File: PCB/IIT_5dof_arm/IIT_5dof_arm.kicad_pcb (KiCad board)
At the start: 2 copper layers, 71.1 x 100 mm, 33 parts, among them J1 Screw_Terminal_01x02, J14 Conn_02x13_Top_Bottom, J8 Conn_01x04, SW1 SW_MAIN, SW15 SW_MOT, U5 XL8574T, U7 SN74LV1T34DBV, U8 SN74LV1T34DBV, U9 4504

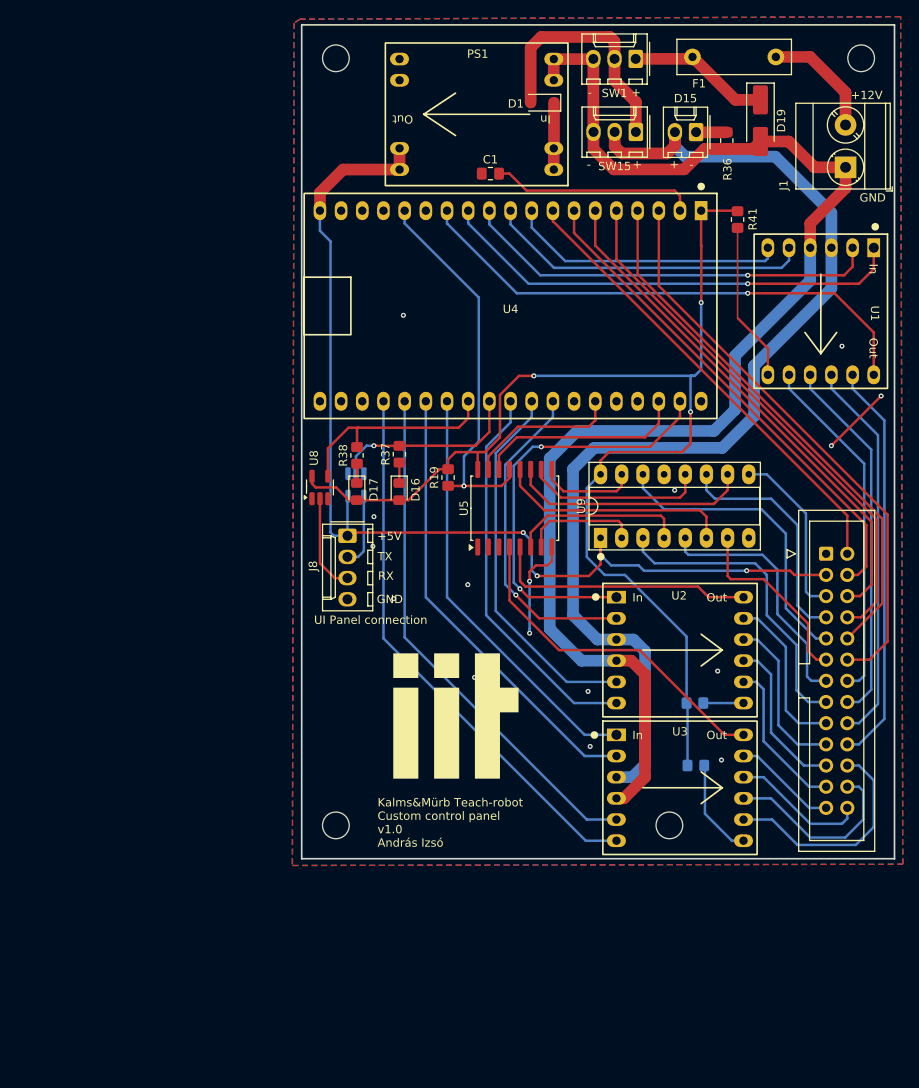
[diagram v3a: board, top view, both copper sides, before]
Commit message: implement RS232
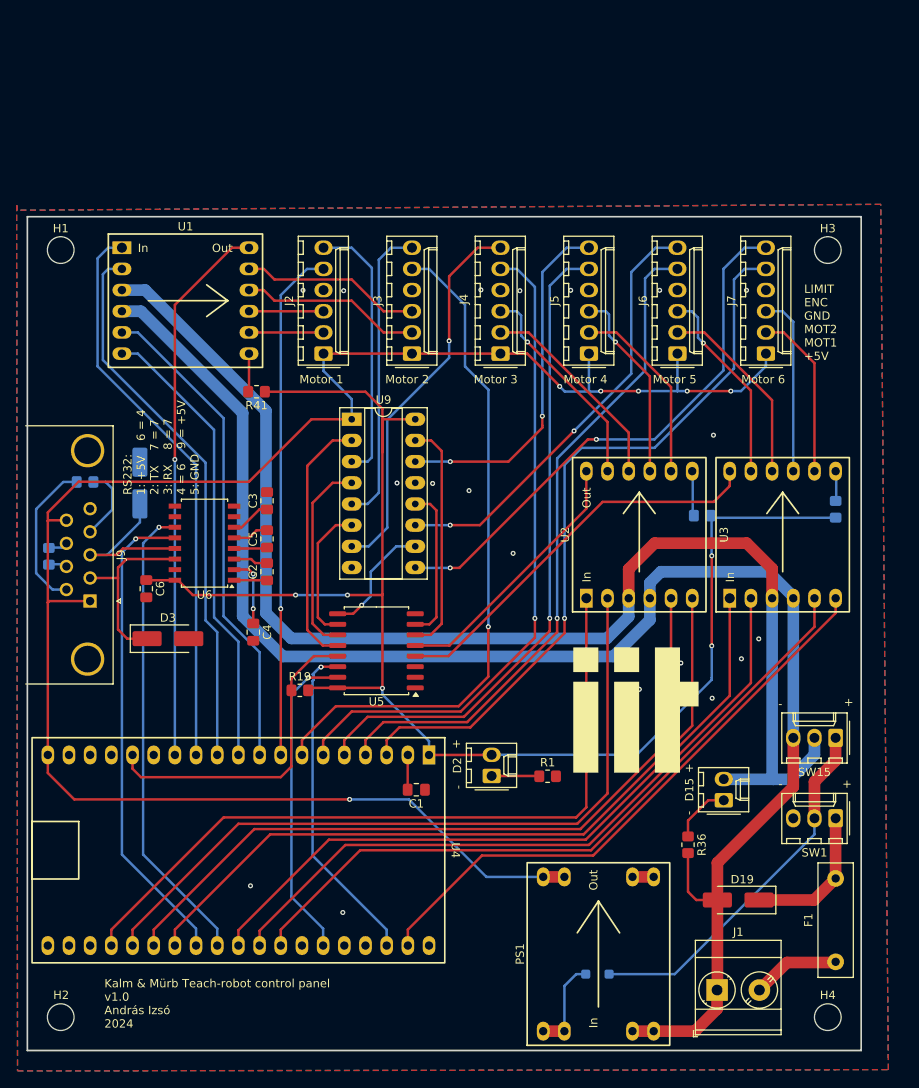
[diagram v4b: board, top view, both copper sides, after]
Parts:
- removed D16, D17: LED, LED_SMD:LED_0805_2012Metric_Pad1.15x1.40mm_HandSolder
- removed J14: Conn_02x13_Top_Bottom, Connector_IDC:IDC-Header_2x13_P2.54mm_Vertical
- removed J8: Conn_01x04, Connector_Molex:Molex_KK-254_AE-6410-04A_1x04_P2.54mm_Vertical
- removed R37, R38: 220, Resistor_SMD:R_0805_2012Metric_Pad1.20x1.40mm_HandSolder
- removed REF** (x4): MountingHole_3.2mm_M3, MountingHole:MountingHole_3.2mm_M3
- removed U7, U8: SN74LV1T34DBV, Package_TO_SOT_SMD:SOT-23-5_HandSoldering
- added C2: 0.1uF, Capacitor_SMD:C_0805_2012Metric_Pad1.18x1.45mm_HandSolder, F.Cu at (78.7, 92.6)
- added C3: 0.1uF, Capacitor_SMD:C_0805_2012Metric_Pad1.18x1.45mm_HandSolder, F.Cu at (78.7, 84.1)
- added C4: 0.1uF, Capacitor_SMD:C_0805_2012Metric_Pad1.18x1.45mm_HandSolder, F.Cu at (77.1, 99.8)
- added C5: 0.1uF, Capacitor_SMD:C_0805_2012Metric_Pad1.18x1.45mm_HandSolder, F.Cu at (78.7, 88.6)
- added C6: 0.1uF, Capacitor_SMD:C_0805_2012Metric_Pad1.18x1.45mm_HandSolder, F.Cu at (64.3, 94.6)
- added D2: LED, Connector_Molex:Molex_KK-254_AE-6410-02A_1x02_P2.54mm_Vertical, F.Cu at (105.7, 117.1)
- added D3: SMAJ12A, Diode_SMD:D_SMA_Handsoldering, F.Cu at (66.9, 100.6)
- added D4: SMAJ12A, Diode_SMD:D_SMA_Handsoldering, B.Cu at (63.5, 81.9)
- added H1: MountingHole, MountingHole:MountingHole_3.2mm_M3, F.Cu at (54.0, 54.0)
- added H2: MountingHole, MountingHole:MountingHole_3.2mm_M3, F.Cu at (54.0, 146.0)
- added H3: MountingHole, MountingHole:MountingHole_3.2mm_M3, F.Cu at (146.0, 54.0)
- added H4: MountingHole, MountingHole:MountingHole_3.2mm_M3, F.Cu at (146.0, 146.0)
- added J2: Conn_01x06, Connector_Molex:Molex_KK-254_AE-6410-06A_1x06_P2.54mm_Vertical, F.Cu at (85.5, 66.4)
- added J3: Conn_01x06, Connector_Molex:Molex_KK-254_AE-6410-06A_1x06_P2.54mm_Vertical, F.Cu at (96.1, 66.4)
- added J4: Conn_01x06, Connector_Molex:Molex_KK-254_AE-6410-06A_1x06_P2.54mm_Vertical, F.Cu at (106.7, 66.4)
- added J5: Conn_01x06, Connector_Molex:Molex_KK-254_AE-6410-06A_1x06_P2.54mm_Vertical, F.Cu at (117.4, 66.4)
- added J6: Conn_01x06, Connector_Molex:Molex_KK-254_AE-6410-06A_1x06_P2.54mm_Vertical, F.Cu at (128.0, 66.4)
- added J7: Conn_01x06, Connector_Molex:Molex_KK-254_AE-6410-06A_1x06_P2.54mm_Vertical, F.Cu at (138.6, 66.4)
- added J9: DE9_Receptacle_MountingHoles, Connector_Dsub:DSUB-9_Female_Horizontal_P2.77x2.84mm_EdgePinOffset4.94mm_Housed_MountingHolesOffset7.48mm, F.Cu at (57.5, 96.1)
- added R1: 220, Resistor_SMD:R_0805_2012Metric_Pad1.20x1.40mm_HandSolder, F.Cu at (112.4, 117.1)
- added R2: 1k, Resistor_SMD:R_0805_2012Metric_Pad1.20x1.40mm_HandSolder, B.Cu at (56.9, 81.8)
- added R3: 1k, Resistor_SMD:R_0805_2012Metric_Pad1.20x1.40mm_HandSolder, B.Cu at (52.6, 90.7)
- added U6: MAX3232, Package_SO:SOIC-16W_5.3x10.2mm_P1.27mm, F.Cu at (71.2, 89.2)
- D1: moved to B.Cu
- moved F1 108.8 mm to (146.9, 139.4), turned to 90 degrees
- moved D1 104.7 mm to (118.4, 140.8), turned to 0 degrees
- moved PS1 101.8 mm to (118.5, 138.4), turned to 90 degrees
- moved J1 99.9 mm to (132.7, 142.7), turned to 0 degrees
- moved SW1 94.2 mm to (146.9, 122.2)
- moved D19 93.5 mm to (135.3, 132.0), turned to 180 degrees
- moved R36 84.6 mm to (129.2, 125.3)
- moved D15 80.2 mm to (133.5, 120.0), turned to 90 degrees
- moved SW15 76.5 mm to (146.9, 112.5)
- moved U1 76.2 mm to (69.0, 60.1), turned to 0 degrees
- moved C1 74.4 mm to (96.6, 118.7), turned to 180 degrees
- moved U4 73.0 mm to (75.3, 126.0)
- moved R41 61.3 mm to (77.5, 71.0), turned to 180 degrees
- moved R43 35.0 mm to (146.9, 85.1), turned to 90 degrees
- moved U9 33.1 mm to (88.9, 74.3), turned to 0 degrees
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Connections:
- SW1 pad 3: GNDPWR -> unconnected-(SW1-C-Pad3)
- U2 pad 1: /mot3_A -> /mot4_A
- U2 pad 10: /Mot4_OUT1 -> /Mot3_OUT1
- U2 pad 11: /Mot4_OUT2 -> /Mot3_OUT2
- U2 pad 2: /mot3_B -> /mot4_B
- U2 pad 5: /mot4_A -> /mot3_A
- U2 pad 6: /mot4_B -> /mot3_B
- U2 pad 8: /Mot3_OUT1 -> /Mot4_OUT1
- U2 pad 9: /Mot3_OUT2 -> /Mot4_OUT2
- U3 pad 10: /Mot6_OUT1 -> /Mot5_OUT1
- U3 pad 11: /Mot6_OUT2 -> /Mot5_OUT2
- U3 pad 8: /Mot5_OUT1 -> /Mot6_OUT1
- U3 pad 9: /Mot5_OUT2 -> /Mot6_OUT2
- U4 pad 10: /mot2_A -> /mot2_B
- U4 pad 23: /mot6_B -> /mot4_A
- U4 pad 24: /mot6_A -> /mot4_B
- U4 pad 25: /mot5_B -> /mot3_A
- U4 pad 26: /mot5_A -> /mot3_B
- U4 pad 29: /mot4_B -> /mot5_A
- U4 pad 3: /Mot5_ENC -> /Mot6_ENC
- U4 pad 30: /mot4_A -> /mot5_B
- U4 pad 31: /mot3_B -> /mot6_A
- U4 pad 37: /mot3_A -> /mot6_B
- U4 pad 4: /Mot6_ENC -> /Mot5_ENC
- U4 pad 5: /Mot3_ENC -> /Mot4_ENC
- U4 pad 6: /Mot4_ENC -> /Mot3_ENC
- U4 pad 7: /Mot1_ENC -> /Mot2_ENC
- U4 pad 8: /Mot2_ENC -> /Mot1_ENC
- U4 pad 9: /mot2_B -> /mot2_A
- U5 pad 10: /Mot5_LIMIT -> /Mot3_LIMIT
- U5 pad 11: /Mot4_LIMIT -> /Mot2_LIMIT
- U5 pad 12: /Mot3_LIMIT -> /Mot1_LIMIT
- U5 pad 6: /Mot2_LIMIT -> /Mot4_LIMIT
- U5 pad 7: /Mot1_LIMIT -> /Mot5_LIMIT
- U9 pad 10: /Mot4_LIMIT -> /Mot6_LIMIT
- U9 pad 14: /Mot6_LIMIT_IN -> /Mot4_LIMIT_IN
- U9 pad 15: /Mot6_LIMIT -> /Mot4_LIMIT
- U9 pad 9: /Mot4_LIMIT_IN -> /Mot6_LIMIT_IN
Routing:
- net +5V: track 130.3 -> 223.4 mm, vias 3 -> 6
- net /mot3_B: track 39.4 -> 89.4 mm, vias 1 -> 0
- net /mot4_A: track 44.9 -> 90.0 mm
- net /mot4_B: track 46.9 -> 89.1 mm
- net /mot3_A: track 51.3 -> 90.3 mm, vias 2 -> 0
- net /Mot1_OUT2: track 44.3 -> 8.94 mm
- net /UI_TX_3v3: track 23.0 -> 56.5 mm
- net /mot5_A: track 50.7 -> 84.1 mm
- net /Mot1_OUT1: track 42.1 -> 8.94 mm
- net /UI_RX_3v3: track 26.1 -> 57.9 mm, vias 0 -> 1
- net GNDPWR: track 162.2 -> 193.1 mm
- net /mot5_B: track 54.2 -> 83.2 mm
- net +3V3: track 148.4 -> 177.0 mm, vias 3 -> 5
- net /Mot6_LIMIT_IN: track 36.3 -> 64.1 mm, vias 0 -> 2
- net /Mot2_OUT2: track 48.6 -> 21.7 mm
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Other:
- board size 71.1 x 100 mm -> 100 x 100 mm
- board text added: "Kalm & Mürb Teach-robot control panel v1.0 András Izsó 2024"
- board text added: "LIMIT ENC GND MOT2 MOT1 +5V"
- board text added: "Motor 1"
- board text added: "Motor 2"
- board text added: "Motor 3"
- board text added: "Motor 4"
- board text added: "Motor 5"
- board text added: "Motor 6"
- board text added: "RS232: 1: +5V 6 = 4 2: TX 7 = 7 3: RX 8 = 7 4 = 6 9 = +5V 5: GND"
- board text removed: "+12V"
- board text removed: "+5V"
- board text removed: "GND"
- board text removed: "Kalms&Mürb Teach-robot Custom control panel v1.0 András Izsó"
- board text removed: "RX"
- board text removed: "TX"
- board text removed: "UI Panel connection"

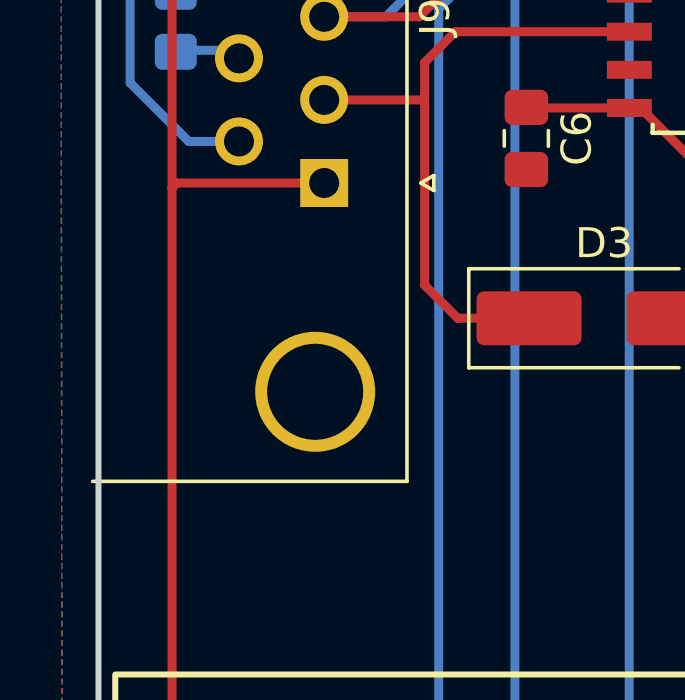
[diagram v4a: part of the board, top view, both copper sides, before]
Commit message: Extend ESD protection on RS-232 interface and tidy up schematic
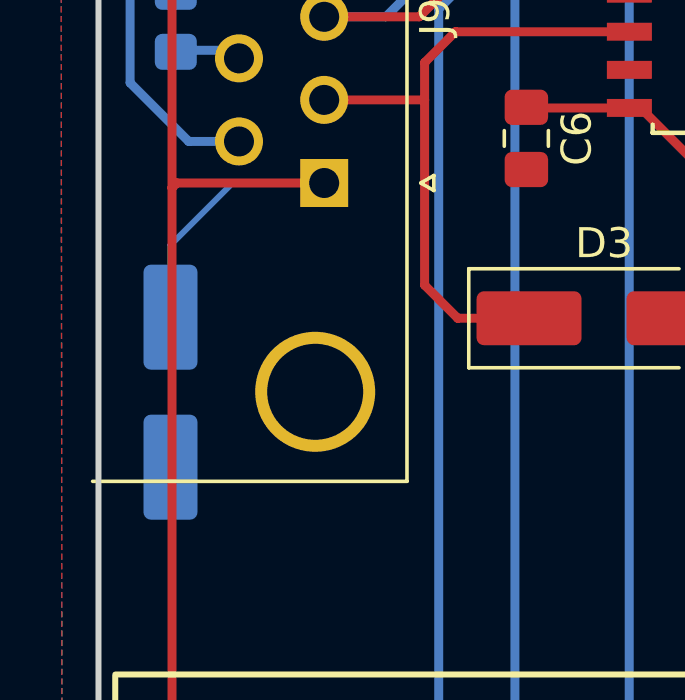
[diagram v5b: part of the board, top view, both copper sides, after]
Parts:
- added D5: SMAJ12A, Diode_SMD:D_SMA_Handsoldering, B.Cu at (52.4, 103.1)
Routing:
- net +5V: track 223.4 -> 231.7 mm

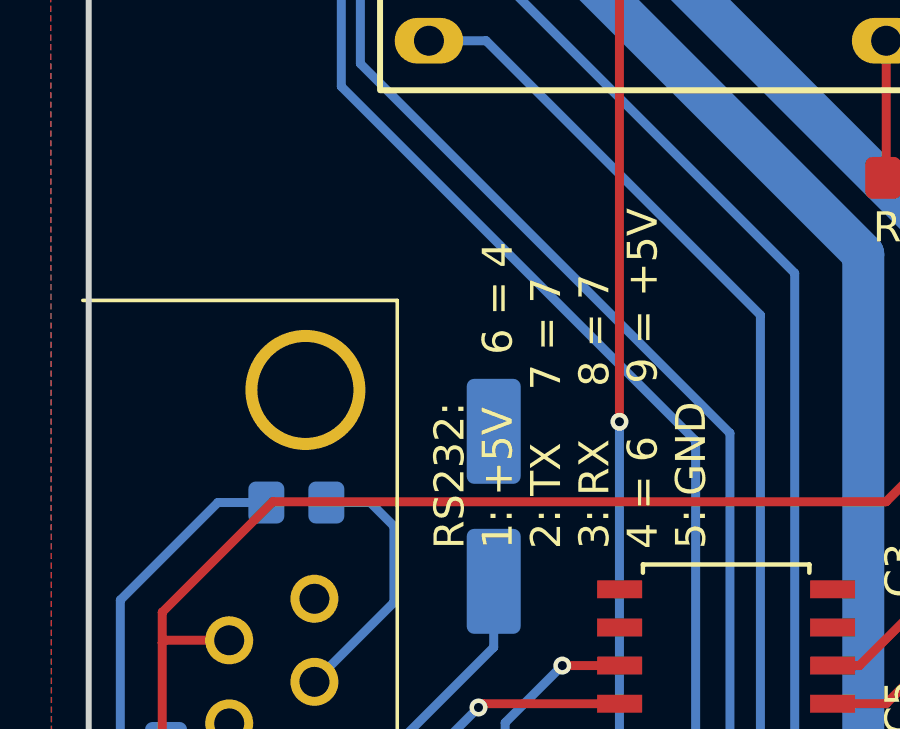
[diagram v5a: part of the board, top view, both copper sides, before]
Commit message: Enhance explanation of control panel RS-232 connections
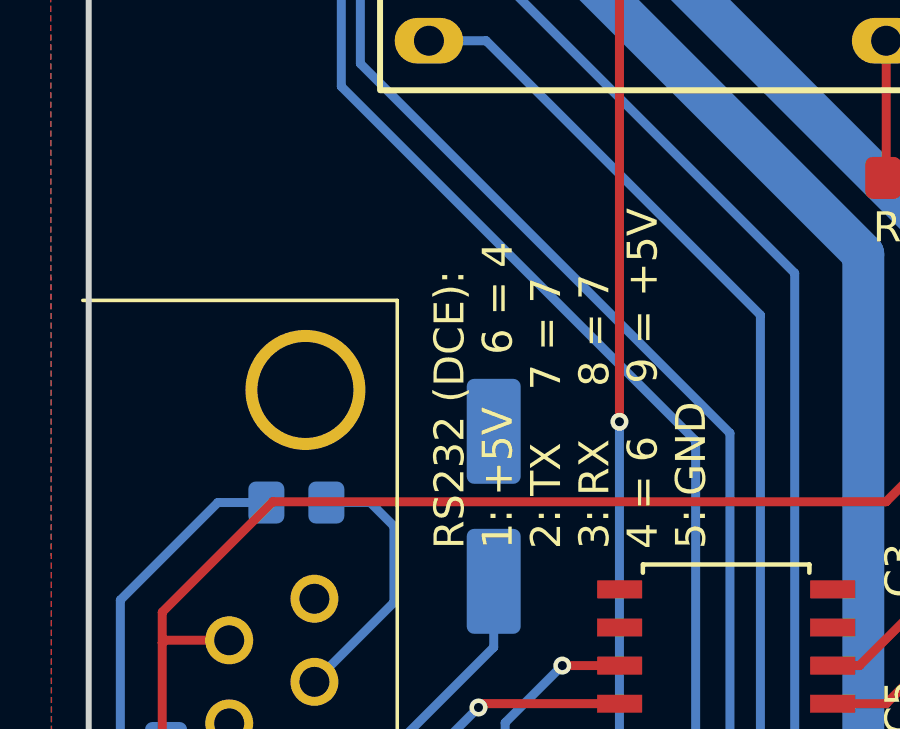
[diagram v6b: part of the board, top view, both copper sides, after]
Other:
- board text added: "RS232 (DCE): 1: +5V 6 = 4 2: TX 7 = 7 3: RX 8 = 7 4 = 6 9 = +5V 5: GND"
- board text removed: "RS232: 1: +5V 6 = 4 2: TX 7 = 7 3: RX 8 = 7 4 = 6 9 = +5V 5: GND"
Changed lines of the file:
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@@
 		(layer "Edge.Cuts")
 	)
-	(gr_text "RS232:\n1: +5V	6 = 4\n2: TX	7 = 7\n3: RX	8 = 7\n4 = 6	9 = +5V\n5: GND	"
+	(gr_text "RS232 (DCE):\n1: +5V	6 = 4\n2: TX	7 = 7\n3: RX	8 = 7\n4 = 6	9 = +5V\n5: GND	"
 		(at 70.6628 83.3628 90)
 		(layer "F.SilkS")

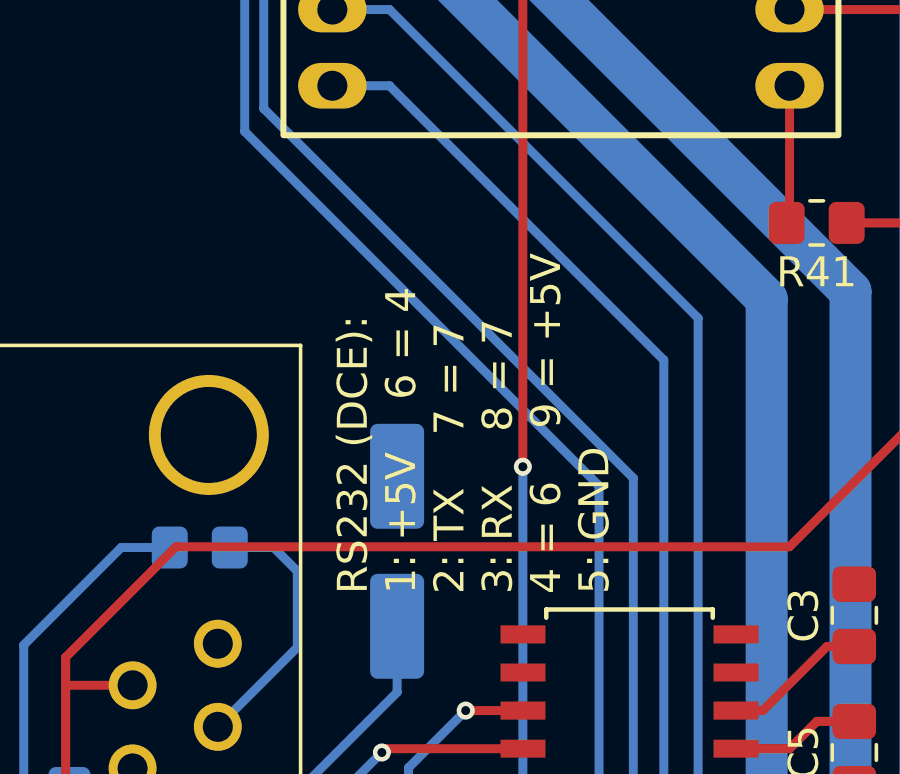
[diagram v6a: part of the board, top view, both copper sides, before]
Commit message: Correct typo in RS232 silkscreen
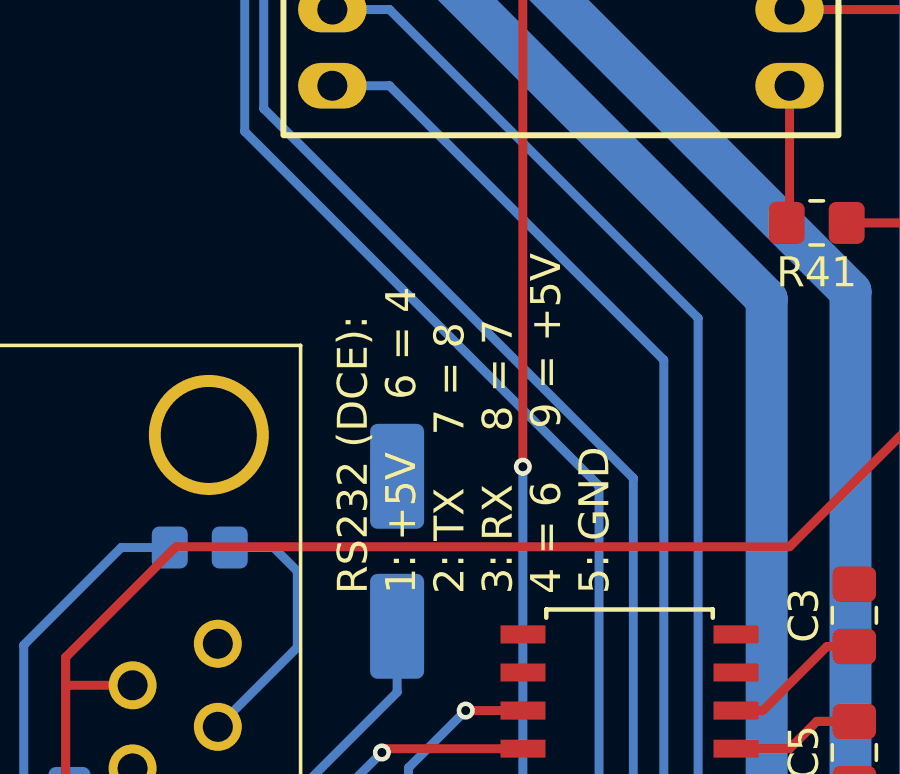
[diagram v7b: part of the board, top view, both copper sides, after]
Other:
- board text added: "RS232 (DCE): 1: +5V 6 = 4 2: TX 7 = 8 3: RX 8 = 7 4 = 6 9 = +5V 5: GND"
- board text removed: "RS232 (DCE): 1: +5V 6 = 4 2: TX 7 = 7 3: RX 8 = 7 4 = 6 9 = +5V 5: GND"
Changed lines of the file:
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@@
 		(layer "Edge.Cuts")
 	)
-	(gr_text "RS232 (DCE):\n1: +5V	6 = 4\n2: TX	7 = 7\n3: RX	8 = 7\n4 = 6	9 = +5V\n5: GND	"
+	(gr_text "RS232 (DCE):\n1: +5V	6 = 4\n2: TX	7 = 8\n3: RX	8 = 7\n4 = 6	9 = +5V\n5: GND	"
 		(at 70.6628 83.3628 90)
 		(layer "F.SilkS")
